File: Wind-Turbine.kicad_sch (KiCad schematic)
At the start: 13 parts

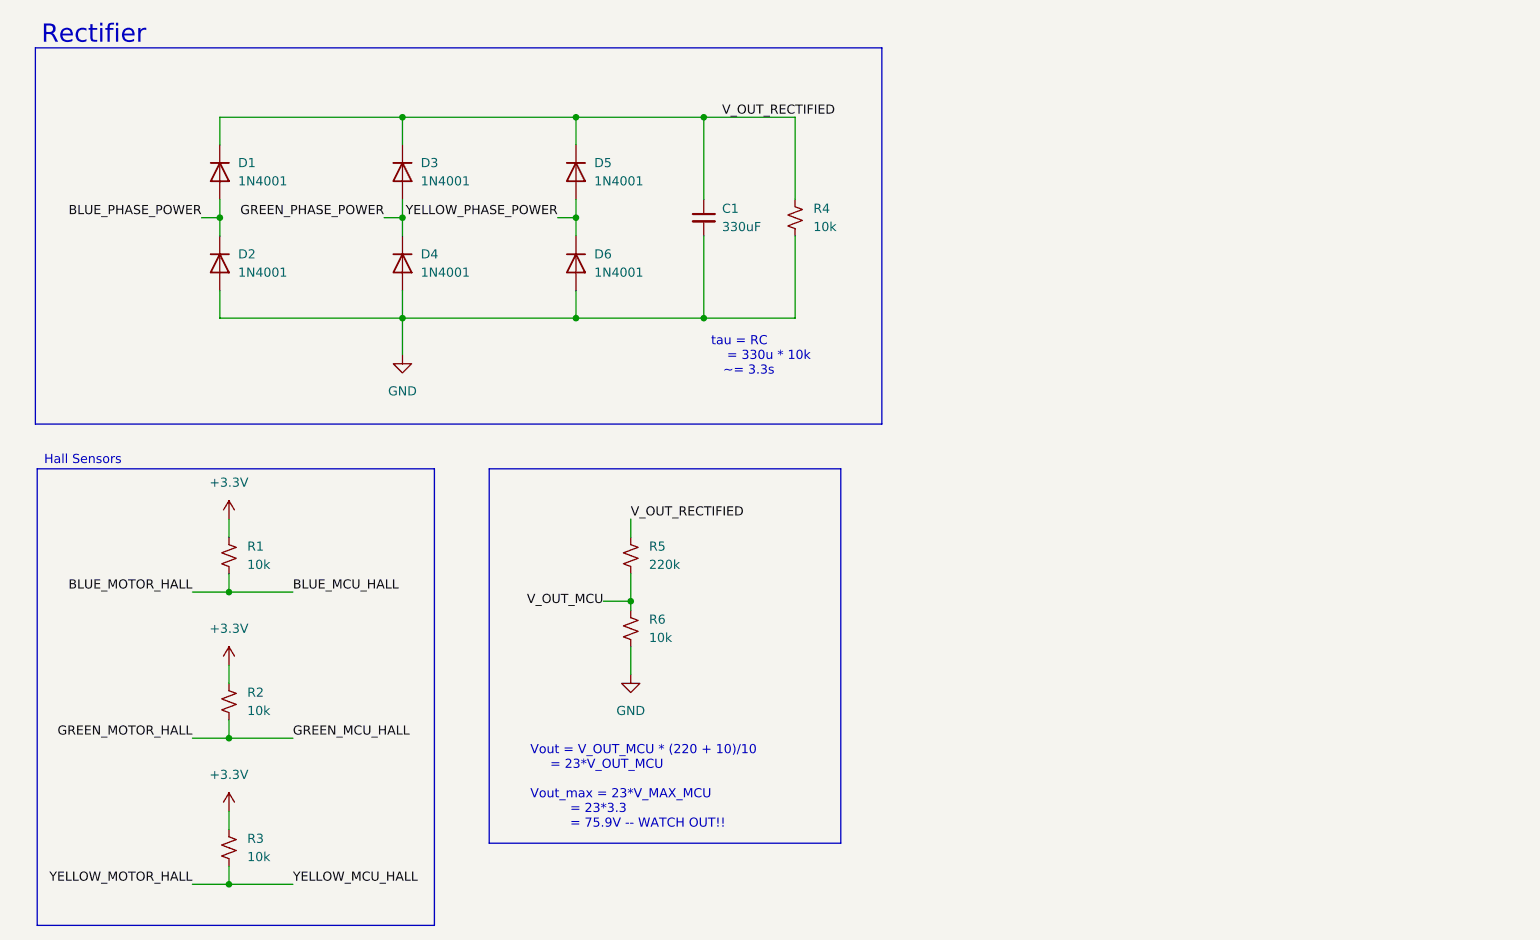
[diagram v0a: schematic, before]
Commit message: Add INA101HP for current monitoring
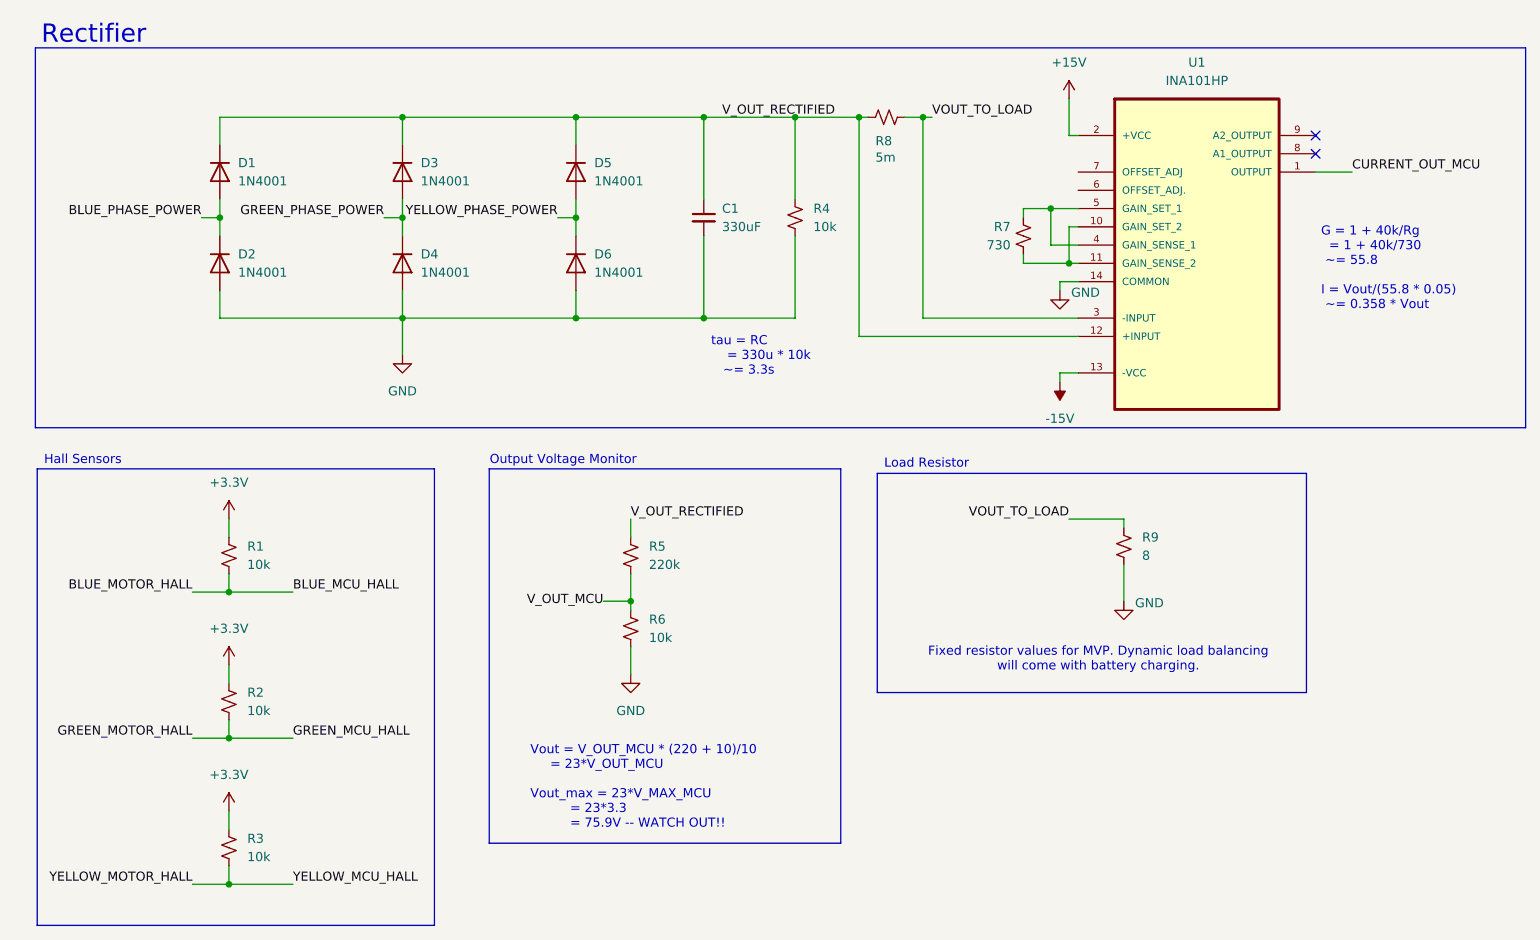
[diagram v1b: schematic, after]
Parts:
- added R7: 730, symbol Device:R_Small_US
- added R8: 5m, symbol Device:R_Small_US
- added R9: 8, symbol Device:R_Small_US
- added U1: INA101HP, INA101HP:DIP254P762X508-14, symbol INA101HP:INA101HP
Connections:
- net GND: now also R9.2, U1.14 (COMMON)
- net V_OUT_RECTIFIED: now also R8.1, U1.12 (+INPUT)
- new net: R7.2, U1.10 (GAIN_SET_2), U1.11 (GAIN_SENSE_2)
- new net: R7.1, U1.4 (GAIN_SENSE_1), U1.5 (GAIN_SET_1)
- new net +15V: U1.2 (+VCC)
- new net -15V: U1.13 (-VCC)
- new net CURRENT_OUT_MCU: U1.1 (OUTPUT)
- new net VOUT_TO_LOAD: R8.2, R9.1, U1.3 (-INPUT)
- no-connect marks 0 -> 2
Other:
- note added: "Fixed resistor values for MVP. Dynamic load balancing will come with battery charging."
- note added: "G = 1 + 40k/Rg = 1 + 40k/730 ~= 55.8 I = Vout/(55.8 * 0.05) ~= 0.358 * Vout"
- note added: "Load Resistor"
- note added: "Output Voltage Monitor"

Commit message: Removed instrmentation op amp
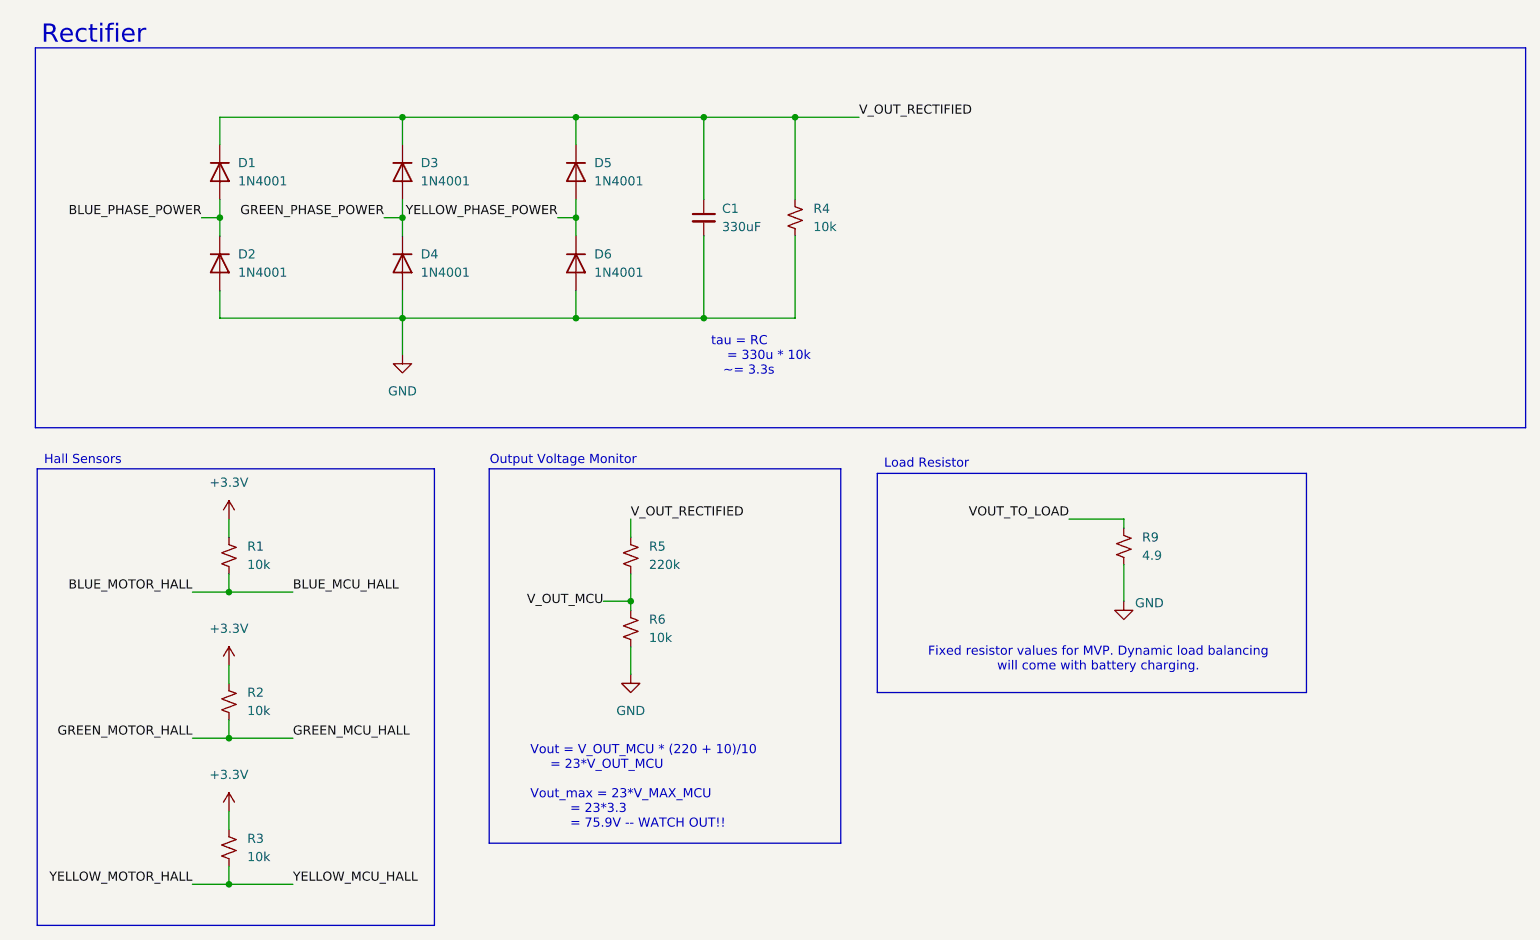
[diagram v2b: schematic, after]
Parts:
- removed R7: 730, symbol Device:R_Small_US
- removed R8: 5m, symbol Device:R_Small_US
- removed U1: INA101HP, INA101HP:DIP254P762X508-14, symbol INA101HP:INA101HP
- R9: value 8 -> 4.9
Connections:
- no-connect marks 2 -> 0
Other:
- note removed: "G = 1 + 40k/Rg = 1 + 40k/730 ~= 55.8 I = Vout/(55.8 * 0.05) ~= 0.358 * Vout"
